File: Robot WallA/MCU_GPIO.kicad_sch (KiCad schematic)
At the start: 2 parts, among them J4 Conn_02x36_Counter_Clockwise, J5 Conn_02x36_Counter_Clockwise

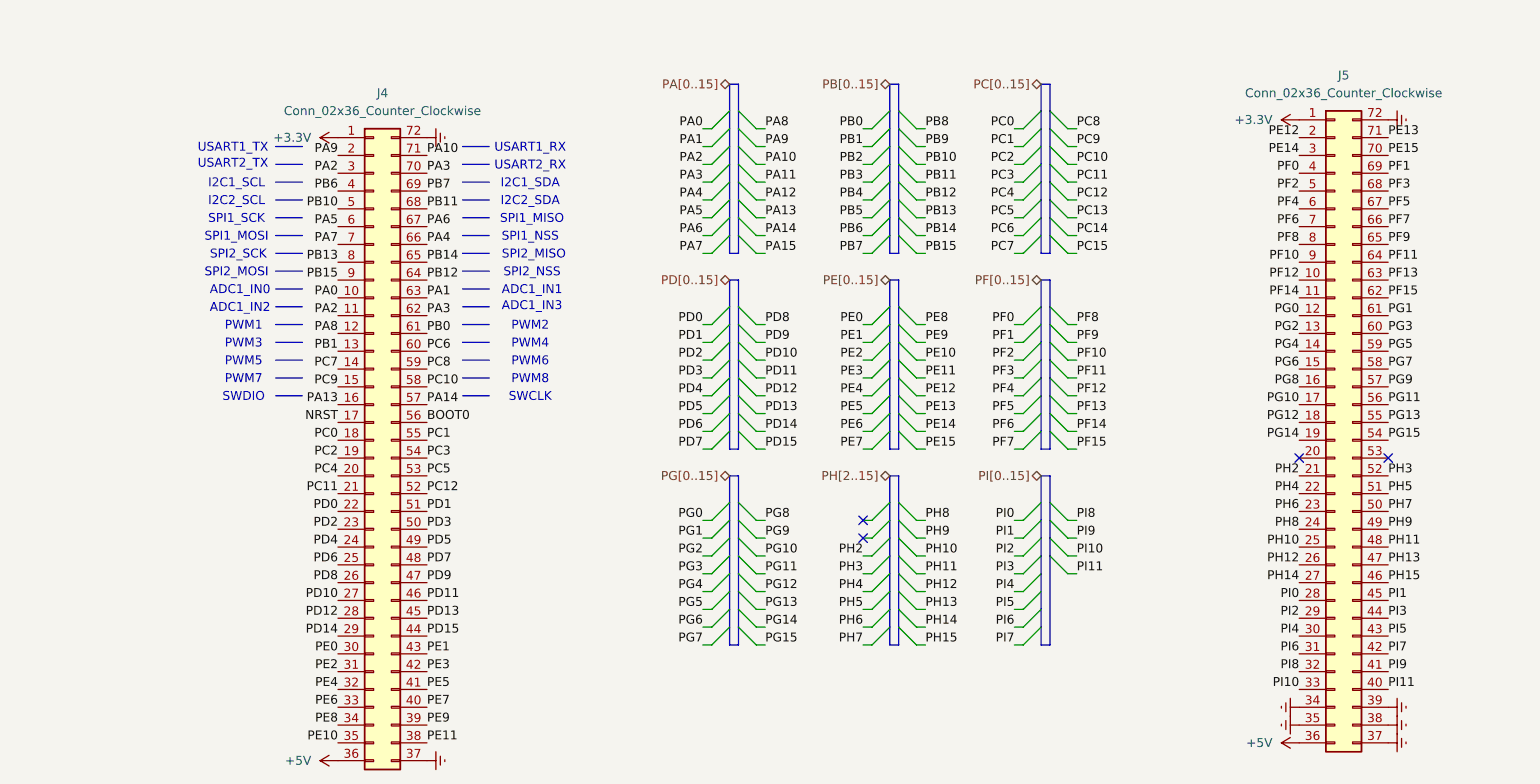
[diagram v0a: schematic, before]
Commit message: Continued to link MCU pins, Added a sheet for servomotors and optional 2 DC motors.
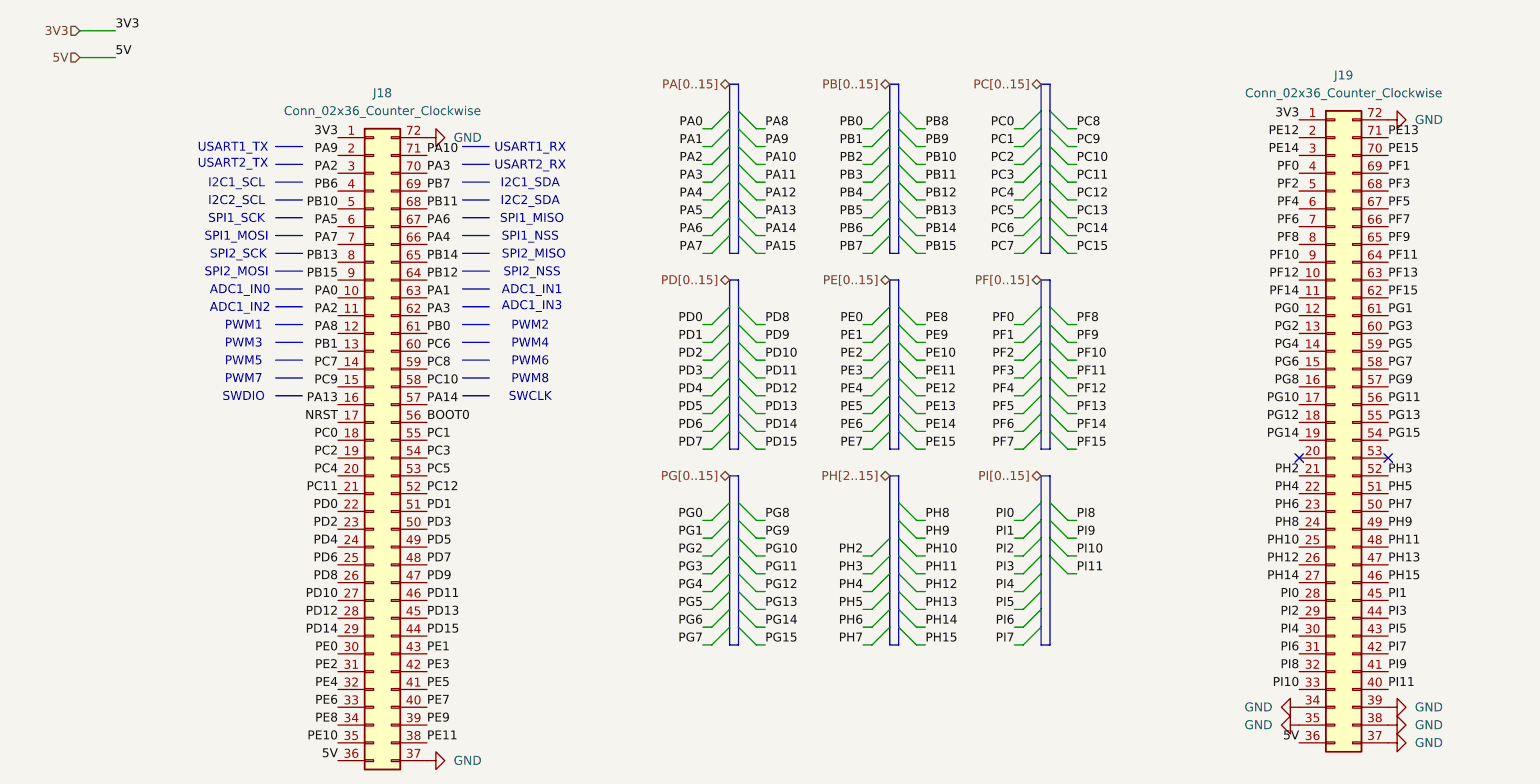
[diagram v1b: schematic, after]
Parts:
- renumbered J4 to J18, J5 to J19
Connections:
- net +3.3V renamed 3V3
- net +5V renamed 5V
- net GNDREF renamed GND
- no-connect marks 4 -> 2

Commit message: Defined every footprints
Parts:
- renumbered J19 to J5, J18 to J6
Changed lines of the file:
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@@
 		(dnp no)
 		(fields_autoplaced yes)
-		(property "Reference" "#PWR028"
+		(property "Reference" "#PWR041"
 			(at 88.9 33.02 0)
 			(effects
@@
 			(project ""
 				(path "/117fd49e-499d-4b54-b58c-f6b538ecca4a/b9176f6a-4299-4bca-a59b-5ff3df09c616/bbbc8572-1c1d-475a-b954-9d9deb469a14"
-					(reference "#PWR028")
+					(reference "#PWR041")
 					(unit 1)
 				)
@@
 		(dnp no)
 		(fields_autoplaced yes)
-		(property "Reference" "J19"
+		(property "Reference" "J5"
 			(at 213.36 24.13 0)
 			(effects
@@
 			(project "PCB"
 				(path "/117fd49e-499d-4b54-b58c-f6b538ecca4a/b9176f6a-4299-4bca-a59b-5ff3df09c616/bbbc8572-1c1d-475a-b954-9d9deb469a14"
-					(reference "J19")
+					(reference "J5")
 					(unit 1)
 				)
@@
 		(dnp no)
 		(fields_autoplaced yes)
-		(property "Reference" "#PWR033"
+		(property "Reference" "#PWR043"
 			(at 226.06 114.3 0)
 			(effects
@@
 			(project "Robot WallA"
 				(path "/117fd49e-499d-4b54-b58c-f6b538ecca4a/b9176f6a-4299-4bca-a59b-5ff3df09c616/bbbc8572-1c1d-475a-b954-9d9deb469a14"
-					(reference "#PWR033")
+					(reference "#PWR043")
 					(unit 1)
 				)
@@
 		(dnp no)
 		(fields_autoplaced yes)
-		(property "Reference" "#PWR029"
+		(property "Reference" "#PWR047"
 			(at 88.9 121.92 0)
 			(effects
@@
 			(project "Robot WallA"
 				(path "/117fd49e-499d-4b54-b58c-f6b538ecca4a/b9176f6a-4299-4bca-a59b-5ff3df09c616/bbbc8572-1c1d-475a-b954-9d9deb469a14"
-					(reference "#PWR029")
+					(reference "#PWR047")
 					(unit 1)
 				)
@@
 		(dnp no)
 		(fields_autoplaced yes)
-		(property "Reference" "#PWR031"
+		(property "Reference" "#PWR044"
 			(at 200.66 116.84 0)
 			(effects
@@
 			(project "Robot WallA"
 				(path "/117fd49e-499d-4b54-b58c-f6b538ecca4a/b9176f6a-4299-4bca-a59b-5ff3df09c616/bbbc8572-1c1d-475a-b954-9d9deb469a14"
-					(reference "#PWR031")
+					(reference "#PWR044")
 					(unit 1)
 				)
@@
 		(dnp no)
 		(fields_autoplaced yes)
-		(property "Reference" "J18"
+		(property "Reference" "J6"
 			(at 76.2 26.67 0)
 			(effects
@@
 			(project "PCB"
 				(path "/117fd49e-499d-4b54-b58c-f6b538ecca4a/b9176f6a-4299-4bca-a59b-5ff3df09c616/bbbc8572-1c1d-475a-b954-9d9deb469a14"
-					(reference "J18")
+					(reference "J6")
 					(unit 1)
 				)
@@
 		(dnp no)
 		(fields_autoplaced yes)
-		(property "Reference" "#PWR035"
+		(property "Reference" "#PWR046"
 			(at 226.06 119.38 0)
 			(effects
@@
 			(project "Robot WallA"
 				(path "/117fd49e-499d-4b54-b58c-f6b538ecca4a/b9176f6a-4299-4bca-a59b-5ff3df09c616/bbbc8572-1c1d-475a-b954-9d9deb469a14"
-					(reference "#PWR035")
+					(reference "#PWR046")
 					(unit 1)
 				)
@@
 		(dnp no)
 		(fields_autoplaced yes)
-		(property "Reference" "#PWR030"
+		(property "Reference" "#PWR042"
 			(at 200.66 114.3 0)
 			(effects
@@
 			(project "Robot WallA"
 				(path "/117fd49e-499d-4b54-b58c-f6b538ecca4a/b9176f6a-4299-4bca-a59b-5ff3df09c616/bbbc8572-1c1d-475a-b954-9d9deb469a14"
-					(reference "#PWR030")
+					(reference "#PWR042")
 					(unit 1)
 				)
@@
 		(dnp no)
 		(fields_autoplaced yes)
-		(property "Reference" "#PWR034"
+		(property "Reference" "#PWR045"
 			(at 226.06 116.84 0)
 			(effects
@@
 			(project "Robot WallA"
 				(path "/117fd49e-499d-4b54-b58c-f6b538ecca4a/b9176f6a-4299-4bca-a59b-5ff3df09c616/bbbc8572-1c1d-475a-b954-9d9deb469a14"
-					(reference "#PWR034")
+					(reference "#PWR045")
 					(unit 1)
 				)
@@
 		(dnp no)
 		(fields_autoplaced yes)
-		(property "Reference" "#PWR032"
+		(property "Reference" "#PWR040"
 			(at 226.06 30.48 0)
 			(effects
@@
 			(project "Robot WallA"
 				(path "/117fd49e-499d-4b54-b58c-f6b538ecca4a/b9176f6a-4299-4bca-a59b-5ff3df09c616/bbbc8572-1c1d-475a-b954-9d9deb469a14"
-					(reference "#PWR032")
+					(reference "#PWR040")
 					(unit 1)
 				)

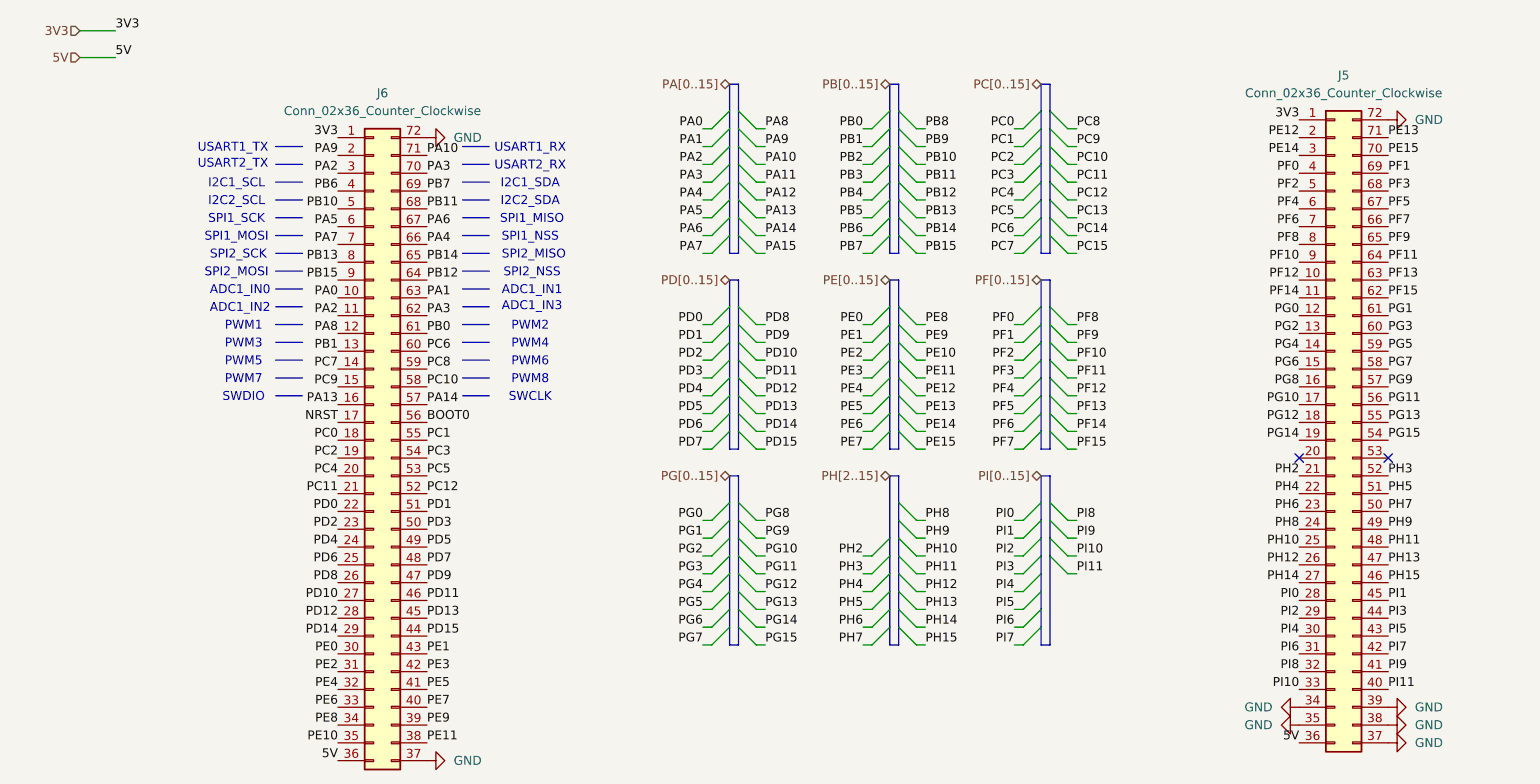
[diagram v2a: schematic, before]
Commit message: Begin to route ethenet, usb, 24V power supply.
Reworked Ethernet sheet because it was too hard to read
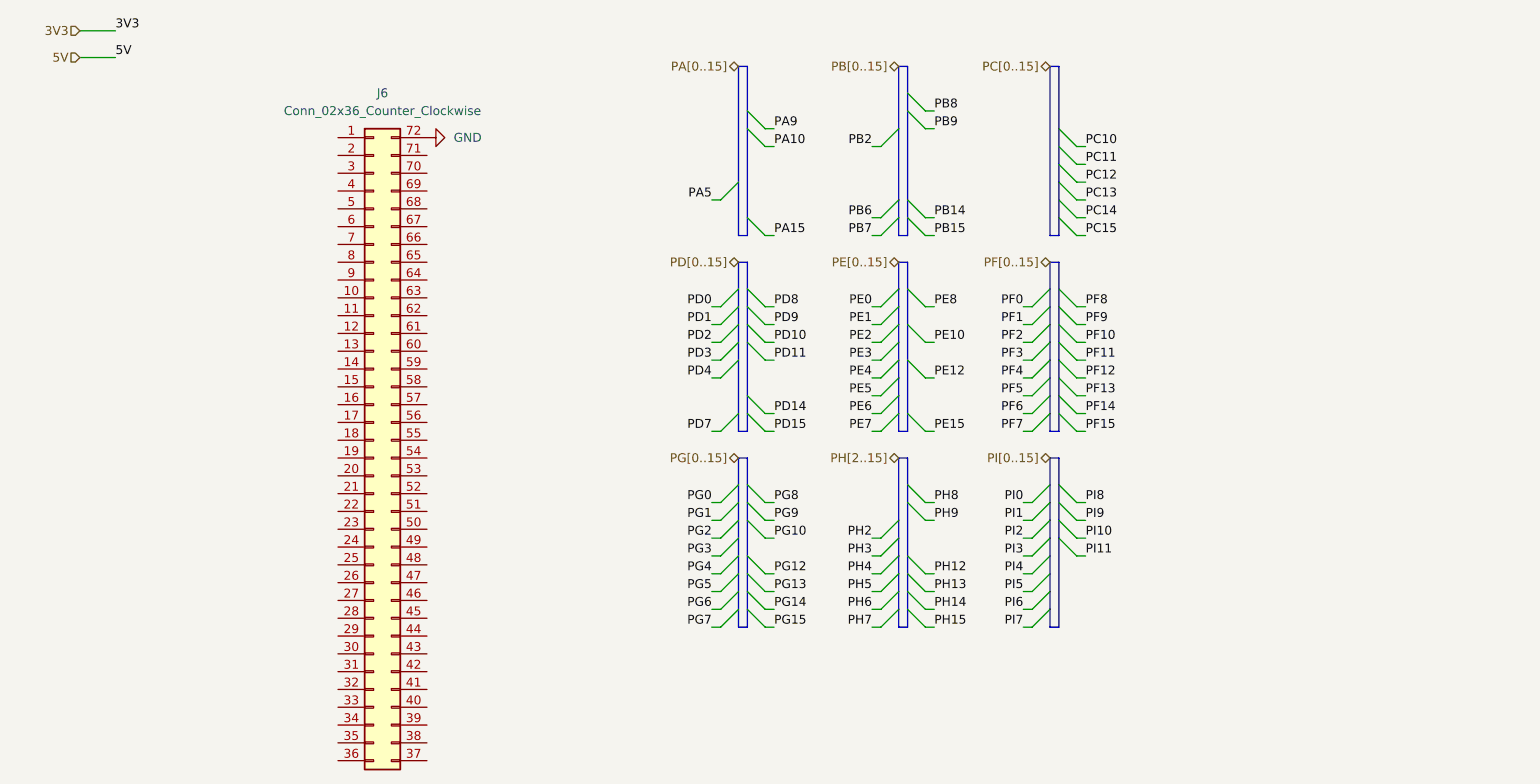
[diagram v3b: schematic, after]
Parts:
- removed J5: Conn_02x36_Counter_Clockwise, Connector_PinHeader_2.54mm:PinHeader_2x36_P2.54mm_Vertical, symbol Connector_Generic:Conn_02x36_Counter_Clockwise
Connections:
- net 3V3: no longer J6.1 (Pin_1)
- net 5V: no longer J6.36 (Pin_36)
- net GND: no longer J6.37 (Pin_37)
- net PA10: no longer J6.71 (Pin_71)
- net PA5: no longer J6.6 (Pin_6)
- net PA9: no longer J6.2 (Pin_2)
- net PB14: no longer J6.65 (Pin_65)
- net PB15: no longer J6.9 (Pin_9)
- net PB6: no longer J6.4 (Pin_4)
- net PB7: no longer J6.69 (Pin_69)
- net PC10: no longer J6.58 (Pin_58)
- net PC11: no longer J6.21 (Pin_21)
- net PC12: no longer J6.52 (Pin_52)
- net PD0: no longer J6.22 (Pin_22)
- net PD1: no longer J6.51 (Pin_51)
- net PD10: no longer J6.27 (Pin_27)
- net PD11: no longer J6.46 (Pin_46)
- net PD14: no longer J6.29 (Pin_29)
- net PD15: no longer J6.44 (Pin_44)
- net PD2: no longer J6.23 (Pin_23)
- net PD3: no longer J6.50 (Pin_50)
- net PD4: no longer J6.24 (Pin_24)
- net PD7: no longer J6.48 (Pin_48)
- net PD8: no longer J6.26 (Pin_26)
- net PD9: no longer J6.47 (Pin_47)
- net PE0: no longer J6.30 (Pin_30)
- net PE1: no longer J6.43 (Pin_43)
- net PE10: no longer J6.35 (Pin_35)
- net PE2: no longer J6.31 (Pin_31)
- net PE3: no longer J6.42 (Pin_42)
- net PE4: no longer J6.32 (Pin_32)
- net PE5: no longer J6.41 (Pin_41)
- net PE6: no longer J6.33 (Pin_33)
- net PE7: no longer J6.40 (Pin_40)
- net PE8: no longer J6.34 (Pin_34)
- net BOOT0: no longer names the net of J6.56 (Pin_56)
- net NRST: no longer names the net of J6.17 (Pin_17)
- net PA0: no longer names the net of J6.10 (Pin_10)
- net PA1: no longer names the net of J6.63 (Pin_63)
- net PA13: no longer names the net of J6.16 (Pin_16)
- net PA14: no longer names the net of J6.57 (Pin_57)
- net PA2: no longer names the net of J6.11 (Pin_11)
- net PA2: no longer J6.3 (Pin_3)
- net PA3: no longer names the net of J6.62 (Pin_62)
- net PA3: no longer J6.70 (Pin_70)
- net PA4: no longer names the net of J6.66 (Pin_66)
- net PA6: no longer names the net of J6.67 (Pin_67)
- net PA7: no longer names the net of J6.7 (Pin_7)
- net PA8: no longer names the net of J6.12 (Pin_12)
- net PB0: no longer names the net of J6.61 (Pin_61)
- net PB1: no longer names the net of J6.13 (Pin_13)
- net PB10: no longer names the net of J6.5 (Pin_5)
- net PB11: no longer names the net of J6.68 (Pin_68)
- net PB12: no longer names the net of J6.64 (Pin_64)
- net PB13: no longer names the net of J6.8 (Pin_8)
- net PC0: no longer names the net of J6.18 (Pin_18)
- net PC1: no longer names the net of J6.55 (Pin_55)
- net PC2: no longer names the net of J6.19 (Pin_19)
- net PC3: no longer names the net of J6.54 (Pin_54)
- net PC4: no longer names the net of J6.20 (Pin_20)
- net PC5: no longer names the net of J6.53 (Pin_53)
- net PC6: no longer names the net of J6.60 (Pin_60)
- net PC7: no longer names the net of J6.14 (Pin_14)
- net PC8: no longer names the net of J6.59 (Pin_59)
- net PC9: no longer names the net of J6.15 (Pin_15)
- net PD12: no longer names the net of J6.28 (Pin_28)
- net PD13: no longer names the net of J6.45 (Pin_45)
- net PD5: no longer names the net of J6.49 (Pin_49)
- net PD6: no longer names the net of J6.25 (Pin_25)
- net PE11: no longer names the net of J6.38 (Pin_38)
- net PE9: no longer names the net of J6.39 (Pin_39)
- no-connect marks 2 -> 0
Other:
- note removed: "ADC1_IN0"
- note removed: "ADC1_IN1"
- note removed: "ADC1_IN2"
- note removed: "ADC1_IN3"
- note removed: "I2C1_SCL"
- note removed: "I2C1_SDA"
- note removed: "I2C2_SCL"
- note removed: "I2C2_SDA"
- note removed: "PWM1"
- note removed: "PWM2"
- note removed: "PWM3"
- note removed: "PWM4"
- note removed: "PWM5"
- note removed: "PWM6"
- note removed: "PWM7"
- note removed: "PWM8"
- note removed: "SPI1_MISO"
- note removed: "SPI1_MOSI"
- note removed: "SPI1_NSS"
- note removed: "SPI1_SCK"
- note removed: "SPI2_MISO"
- note removed: "SPI2_MOSI"
- note removed: "SPI2_NSS"
- note removed: "SPI2_SCK"
- note removed: "SWCLK"
- note removed: "SWDIO"
- note removed: "USART1_RX"
- note removed: "USART1_TX"
- note removed: "USART2_RX"
- note removed: "USART2_TX"

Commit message: Conitnue routing
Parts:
- removed J6: Conn_02x36_Counter_Clockwise, Connector_PinHeader_2.54mm:PinHeader_2x36_P2.54mm_Vertical, symbol Connector_Generic:Conn_02x36_Counter_Clockwise
- added J5: M20-8762042, SamacSys_Parts:M208762042, symbol SamacSys_new:M20-8762042

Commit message: Correct a lot of error in DRC
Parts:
- added J13, J6: 10129383-916001ALF, 10129383916001ALF, symbol SamacSys_new:10129383-916001ALF
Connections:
- net 3V3: now also J6.B1
- net 5V: now also J6.A1
- net PA0: now also J5.1
- net PA10: now also J5.3
- net PA15: now also J5.4
- net PA9: now also J5.2
- net PB6: now also J5.5
- net PB7: now also J5.6
- net PB8: now also J5.7
- net PB9: now also J5.8
- net PC10: now also J5.9
- net PC11: now also J5.10
- net PC12: now also J5.11
- net PC13: now also J5.12
- net PC14: now also J5.13
- net PC15: now also J5.14
- net PD0: now also J5.15
- net PD1: now also J5.16
- net PD10: now also J5.23
- net PD11: now also J5.24
- net PD14: now also J5.25
- net PD15: now also J5.26
- net PD2: now also J5.17
- net PD3: now also J5.18
- net PD4: now also J5.19
- net PD7: now also J5.20
- net PD8: now also J5.21
- net PD9: now also J5.22
- net PE0: now also J5.27
- net PE1: now also J5.28
- net PE10: now also J5.36
- net PE12: now also J5.37
- net PE15: now also J5.38
- net PE2: now also J5.29
- net PE3: now also J5.30
- net PE4: now also J5.31
- net PE5: now also J5.32
- net PE6: now also J5.33
- net PE7: now also J5.34
- net PE8: now also J5.35
- net PF0: now also J5.39
- net PF3: now also J5.40
- no-connect marks 0 -> 39
